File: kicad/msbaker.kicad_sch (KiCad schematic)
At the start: 13 parts

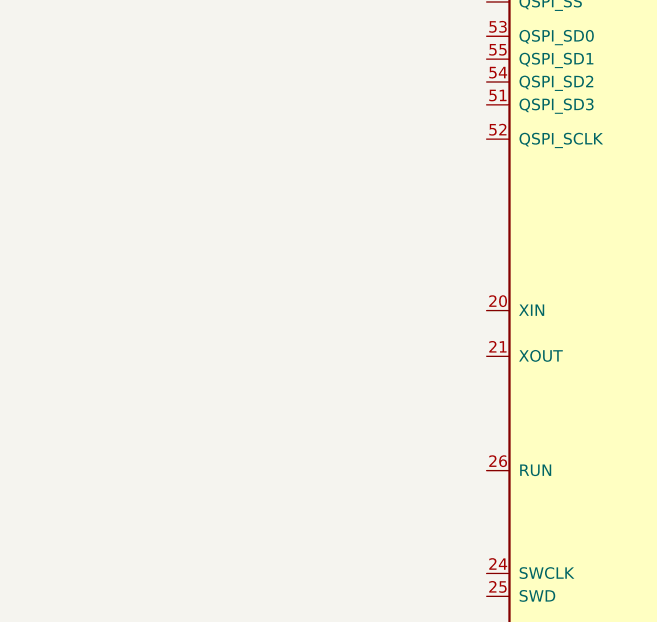
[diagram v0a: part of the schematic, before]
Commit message: Added clock crystal block
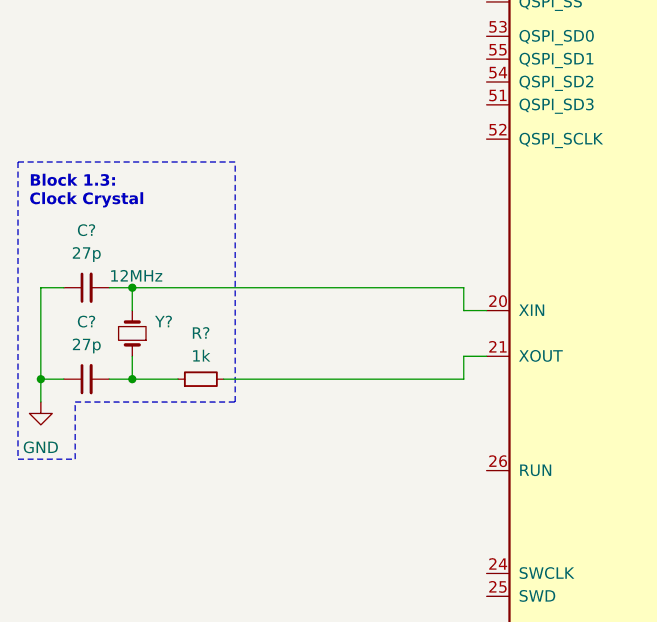
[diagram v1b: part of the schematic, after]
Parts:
- added C? (x2): 27p, symbol Device:C_Small
- added R?: 1k, symbol Device:R_Small
- added Y?: 12MHz, symbol Device:Crystal_Small
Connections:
- net GND: now also C?.1, C?.1
- net at U?.20 (XIN): now also C?.2, Y?.2
- net at U?.21 (XOUT): now also R?.2
- new net: C?.2, R?.1, Y?.1
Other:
- note added: "Block 1.3: Clock Crystal"

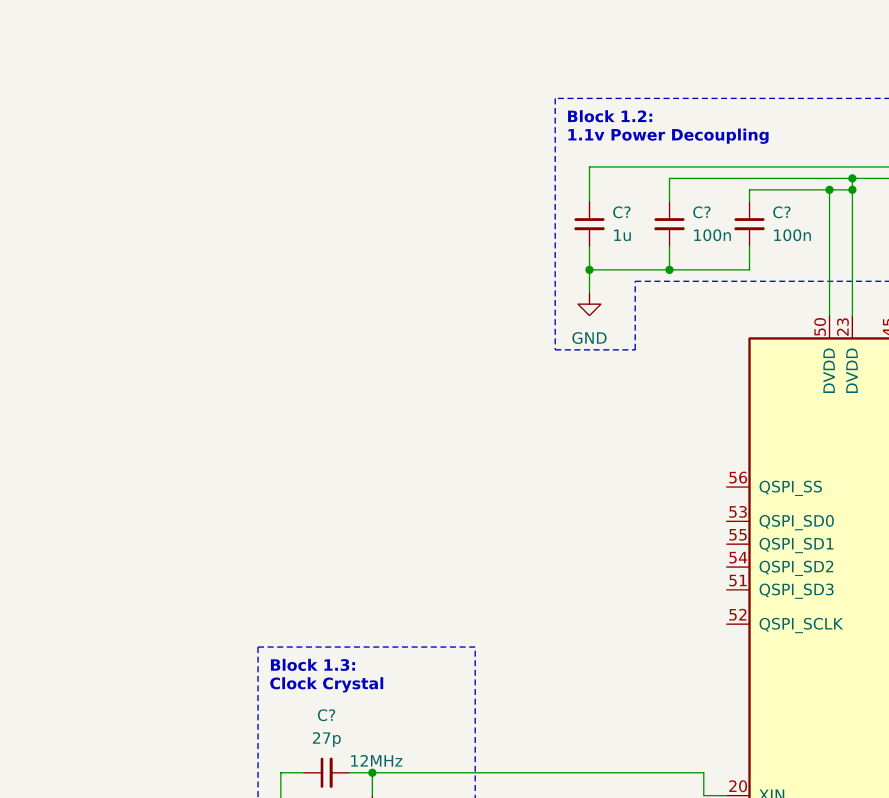
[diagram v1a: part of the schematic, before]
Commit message: Added flash memory block
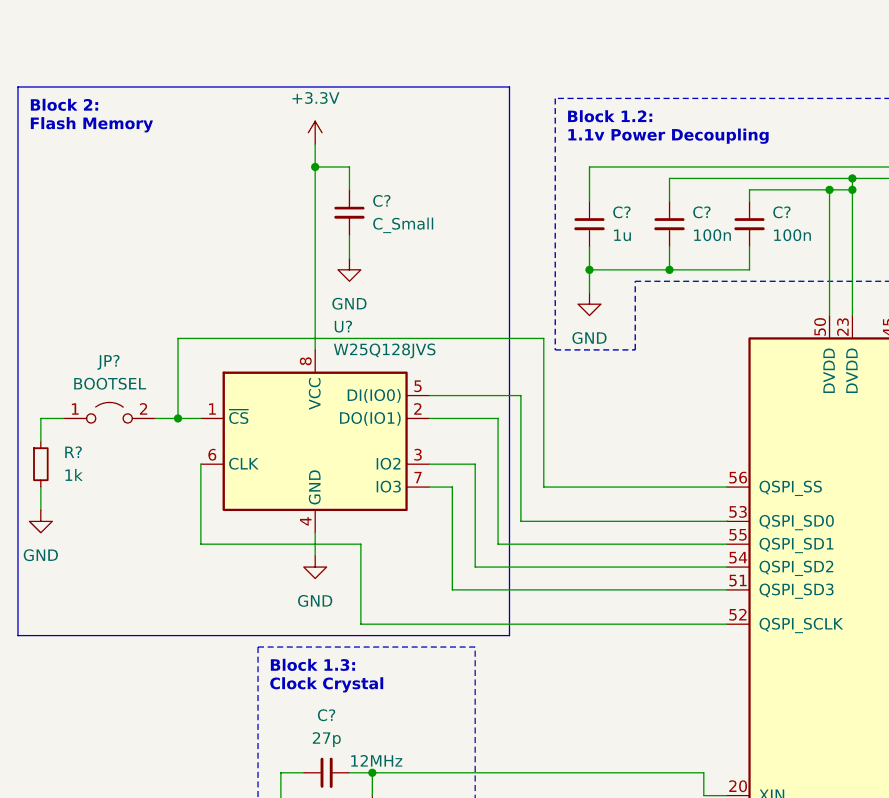
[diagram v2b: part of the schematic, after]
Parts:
- added C?: C_Small, symbol Device:C_Small
- added JP?: BOOTSEL, symbol Jumper:Jumper_2_Open
- added R?: 1k, symbol Device:R_Small
- added U?: W25Q128JVS, Package_SO:SOIC-8_5.23x5.23mm_P1.27mm, symbol Memory_Flash:W25Q128JVS
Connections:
- net +3.3V: now also C?.1, U?.8 (VCC)
- net GND: now also C?.2, R?.2, U?.4 (GND)
- net at U?.51 (QSPI_SD3): now also U?.7 (IO3)
- net at U?.52 (QSPI_SCLK): now also U?.6 (CLK)
- net at U?.53 (QSPI_SD0): now also U?.5 (DI(IO0))
- net at U?.54 (QSPI_SD2): now also U?.3 (IO2)
- net at U?.55 (QSPI_SD1): now also U?.2 (DO(IO1))
- net at U?.56 (QSPI_SS): now also JP?.2 (B), U?.1 (~{CS})
- new net: JP?.1 (A), R?.1
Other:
- note added: "Block 2: Flash Memory"

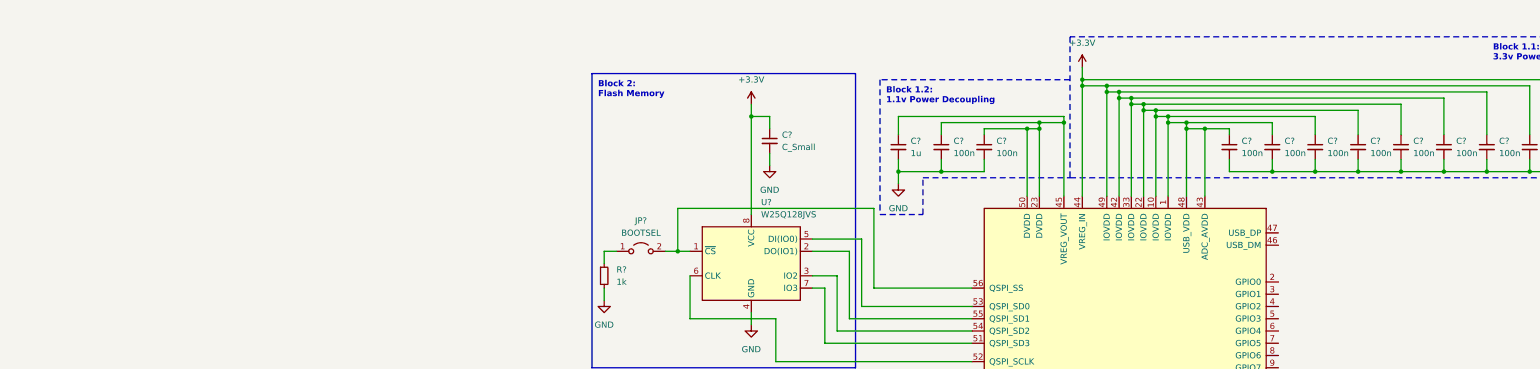
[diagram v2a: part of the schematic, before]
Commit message: Added 3.3v power supply block
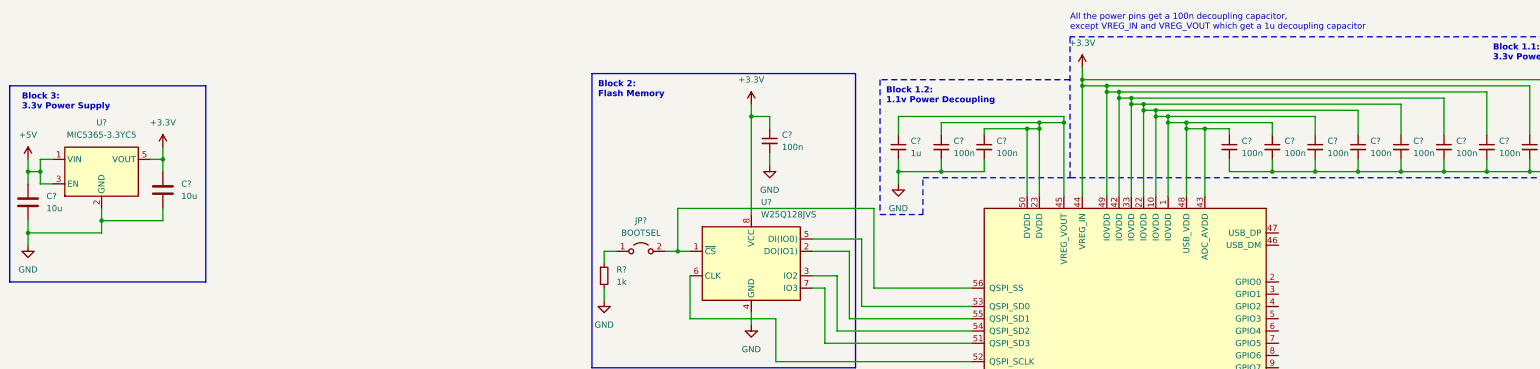
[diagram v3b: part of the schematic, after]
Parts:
- added C? (x2): 10u, symbol Device:C
- added U?: MIC5365-3.3YC5, Package_TO_SOT_SMD:SOT-353_SC-70-5, symbol Regulator_Linear:MIC5365-3.3YC5
- C?: value C_Small -> 100n
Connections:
- net +3.3V: now also C?.1, U?.5 (VOUT)
- net GND: now also C?.2, C?.2, U?.2 (GND)
- new net +5V: C?.1, U?.1 (VIN), U?.3 (EN)
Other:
- note added: "All the power pins get a 100n decoupling capacitor, except VREG_IN and VREG_VOUT which get a 1u decoupling capacitor"
- note added: "Block 3: 3.3v Power Supply"

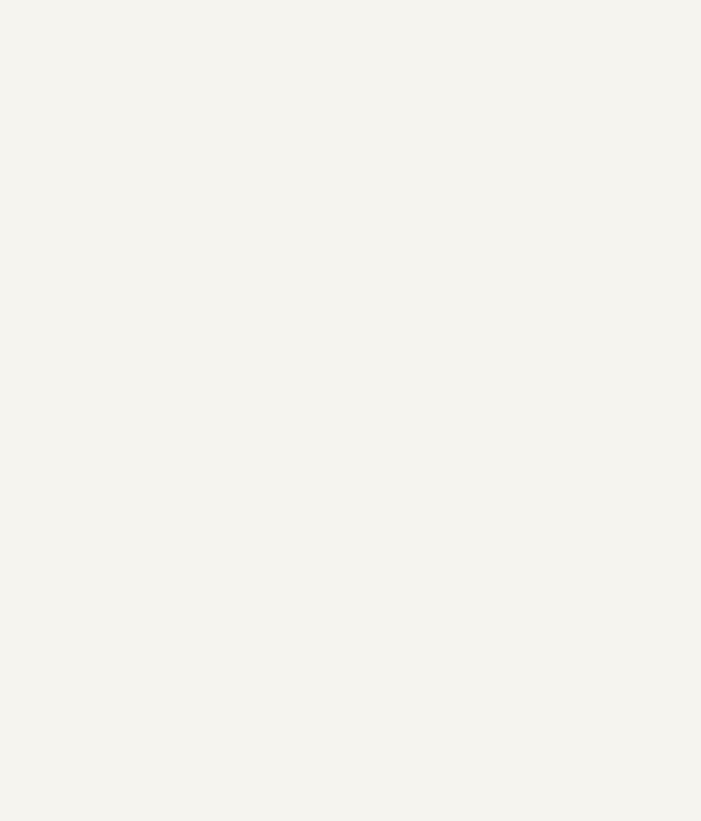
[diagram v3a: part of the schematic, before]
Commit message: Added imu block
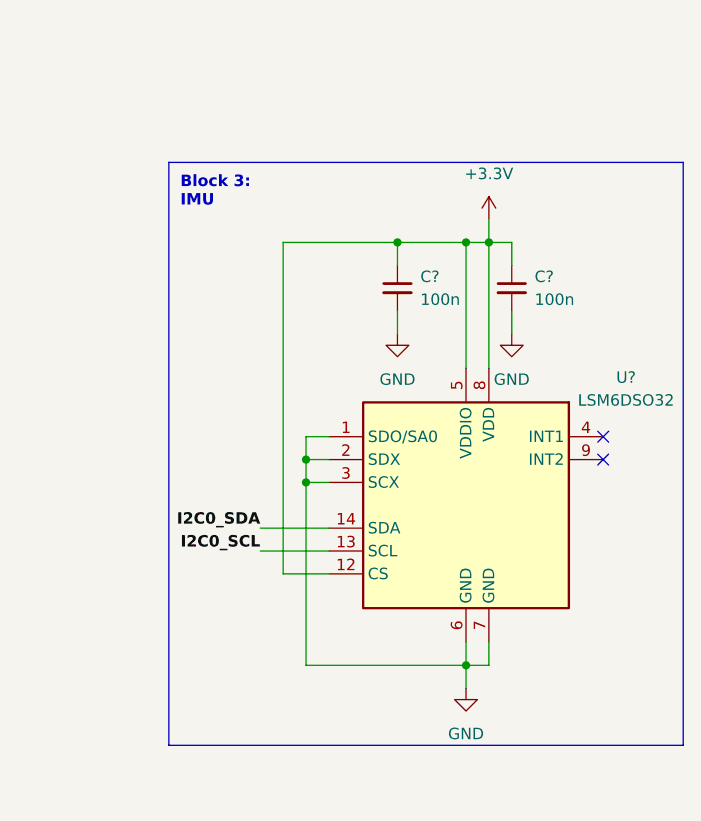
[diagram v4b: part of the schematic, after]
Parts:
- added C? (x2): 100n, symbol Device:C_Small
- added U?: LSM6DSO32, Package_LGA:LGA-14_3x2.5mm_P0.5mm_LayoutBorder3x4y, symbol Sensor_Motion:LSM6DS3
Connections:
- net +3.3V: now also C?.1, C?.1, U?.12 (CS), U?.5 (VDDIO), U?.8 (VDD)
- net GND: now also C?.2, C?.2, U?.1 (SDO/SA0), U?.2 (SDX), U?.3 (SCX), U?.6 (GND), U?.7 (GND)
- new net I2C0_SCL: U?.13 (SCL)
- new net I2C0_SDA: U?.14 (SDA)
- no-connect marks 0 -> 2
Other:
- note added: "Block 3: IMU"
